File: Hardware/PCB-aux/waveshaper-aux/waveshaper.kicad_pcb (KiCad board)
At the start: 2 copper layers, 189 x 174 mm, 50 parts, among them J1 AudioJack2_SwitchT, J10 2x7 IDC header, J11 Conn_01x03, J12 Conn_01x02, J13 EURO_PWR_2x5, J14 Conn_01x9, J15 Conn_01x9, J2 AudioJack2_SwitchT, J20 Conn_01x02, J3 AudioJack2_SwitchT, J30 2x5 pin socket, J4 AudioJack2_SwitchT, J5 AudioJack2_SwitchT, J6 AudioJack2_SwitchT, J7 AudioJack2_SwitchT, J8 AudioJack2_SwitchT, J9 AudioJack2_SwitchT, SW1 SW_SPDT, U4 4066, U5 4066

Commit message: PCB tweak, font correction on panel
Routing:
- net Net-(D4-Pad2): track 201.4 -> 192.1 mm
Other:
- board text added: "+1"
- board text added: "+10V"
- board text added: "+2"
- board text added: "+3"
- board text added: "-1"
- board text added: "-2"
- board text added: "-3"
- board text added: "0"
- board text added: "GND"

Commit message: Final tweaks before fabbing; Kosmo_panel lib update
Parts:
- added GRAF1: CC0 logo, ao_tht:CC0_logo, B.Cu at (145.5, 55.8)
- renumbered C14 to C1, C15 to C2, C16 to C3, C17 to C4, D4 to D1, D5 to D4, D6 to D5, D7 to D6, D8 to D7, D9 to D8, D10 to D9, J10 to J1, J4 to J10, J5 to J12, J30 to J13, J6 to J14, J7 to J15, J8 to J16, J9 to J17, J1 to J2, J2 to J3, J12 to J4, J13 to J5, J3 to J6, J14 to J7, J20 to J8, J15 to J9, R8 to R1, R9 to R2, R10 to R3, R11 to R4, R12 to R5, R13 to R6, R14 to R7, R25 to R8, R26 to R9, RV8 to RV2, RV2 to RV3, RV3 to RV4, RV4 to RV5, RV5 to RV6, RV6 to RV7, RV7 to RV8, U5 to U1, U4 to U2
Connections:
- J10 pad S: GND -> GND1
- J12 pad S: GND -> GND1
- J14 pad S: GND -> GND1
- J15 pad S: GND -> GND1
- J16 pad S: GND -> GND1
- J17 pad S: GND -> GND1
- J2 pad S: GND -> GND1
- J3 pad S: GND -> GND1
- J6 pad S: GND -> GND1
- J7 pad 1: GND -> GND1
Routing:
- added copper zone on B.Cu, net GND1
- added copper zone on F.Cu, net GND1
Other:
- rule pad_to_mask_clearance: 0.05 -> 0
- board text added: "VCA/pot/switch board Rich Holmes Oct 2020 CC0"
- board text added: "Voltage Controlled 4046 Wave Shaper"
- board text removed: "Voltage Controlled 4046 Wave Shaper VCA/pot/switch board Rich Holmes Oct 2020"

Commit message: Gerbers
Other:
- board text added: "https://github.com/holmesrichards/WaveShaper"

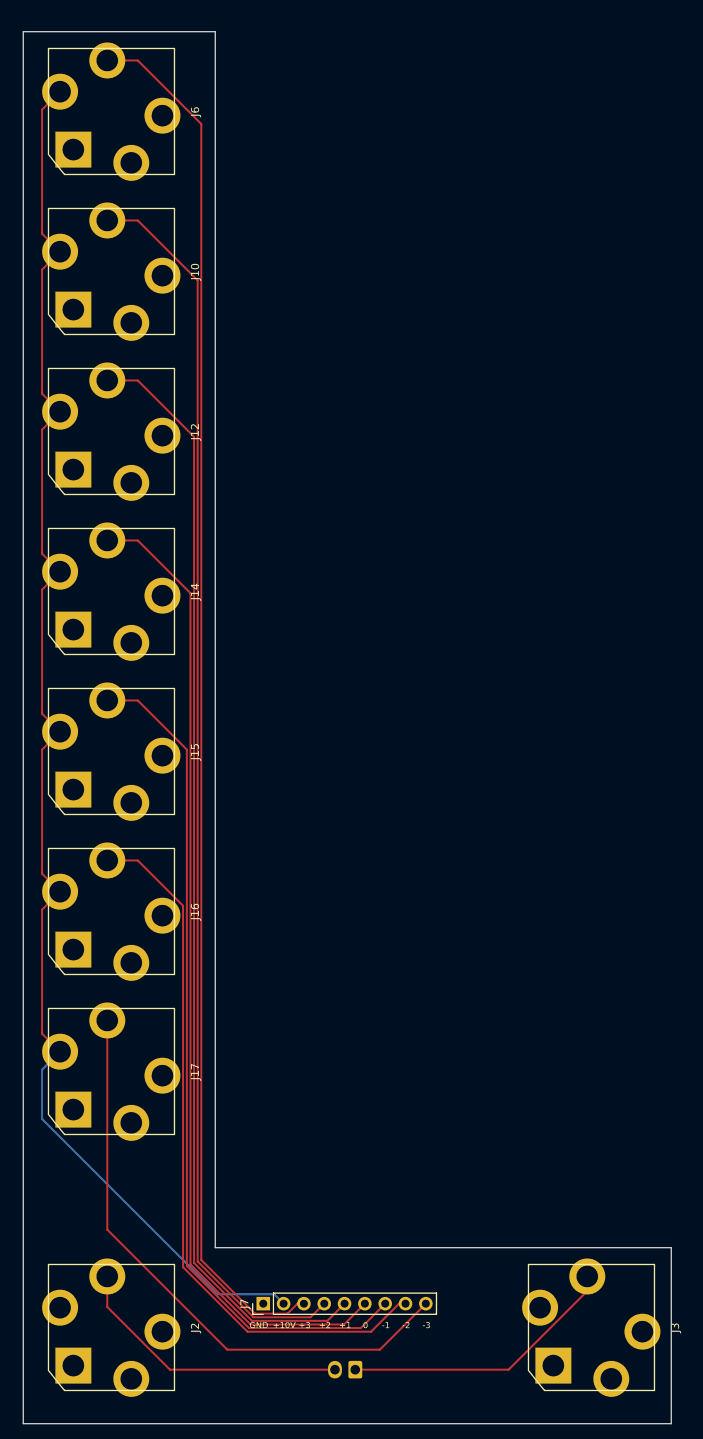
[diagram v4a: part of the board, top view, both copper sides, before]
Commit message: Documentation, some cosmetic sch/PCB changes
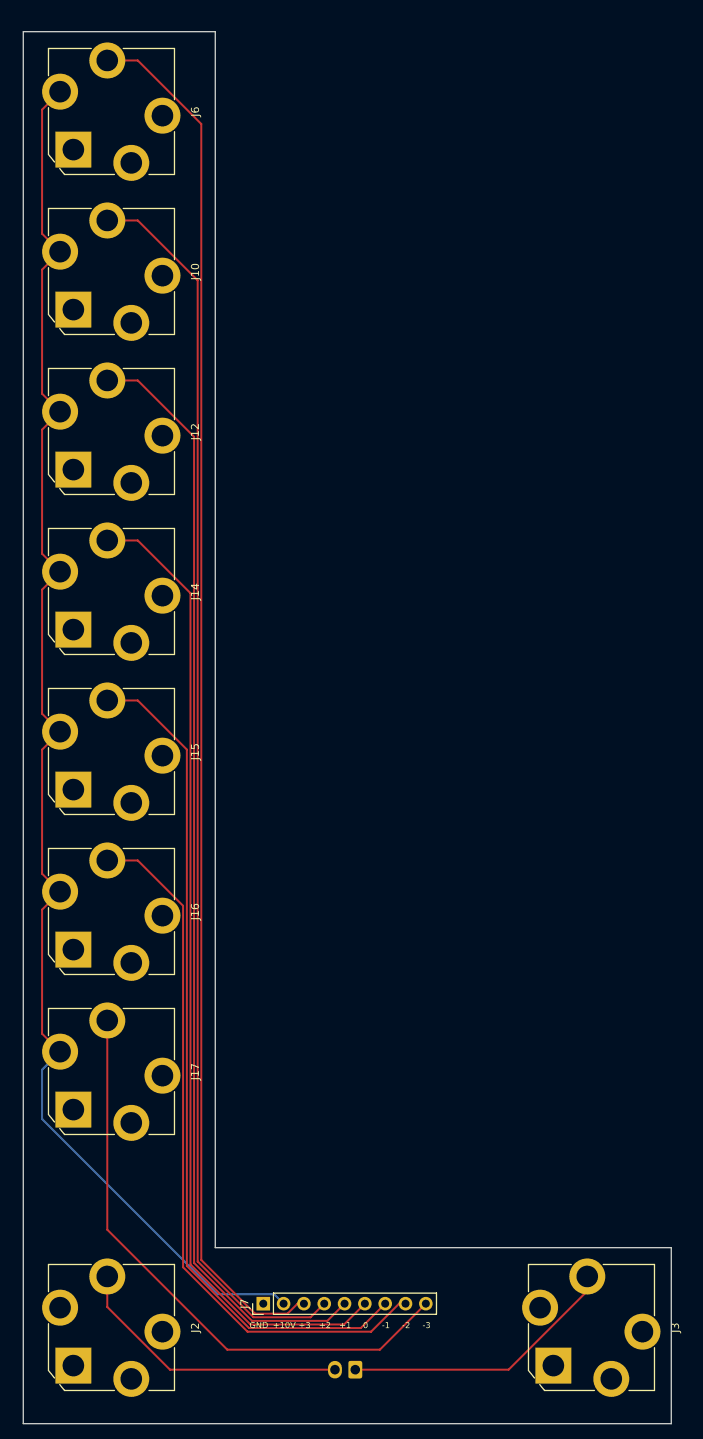
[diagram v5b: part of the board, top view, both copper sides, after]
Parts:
- J11: value Conn_01x03 -> 3_pin_Molex_header
- J4, J8: value Conn_01x02 -> 2_pin_Molex_header

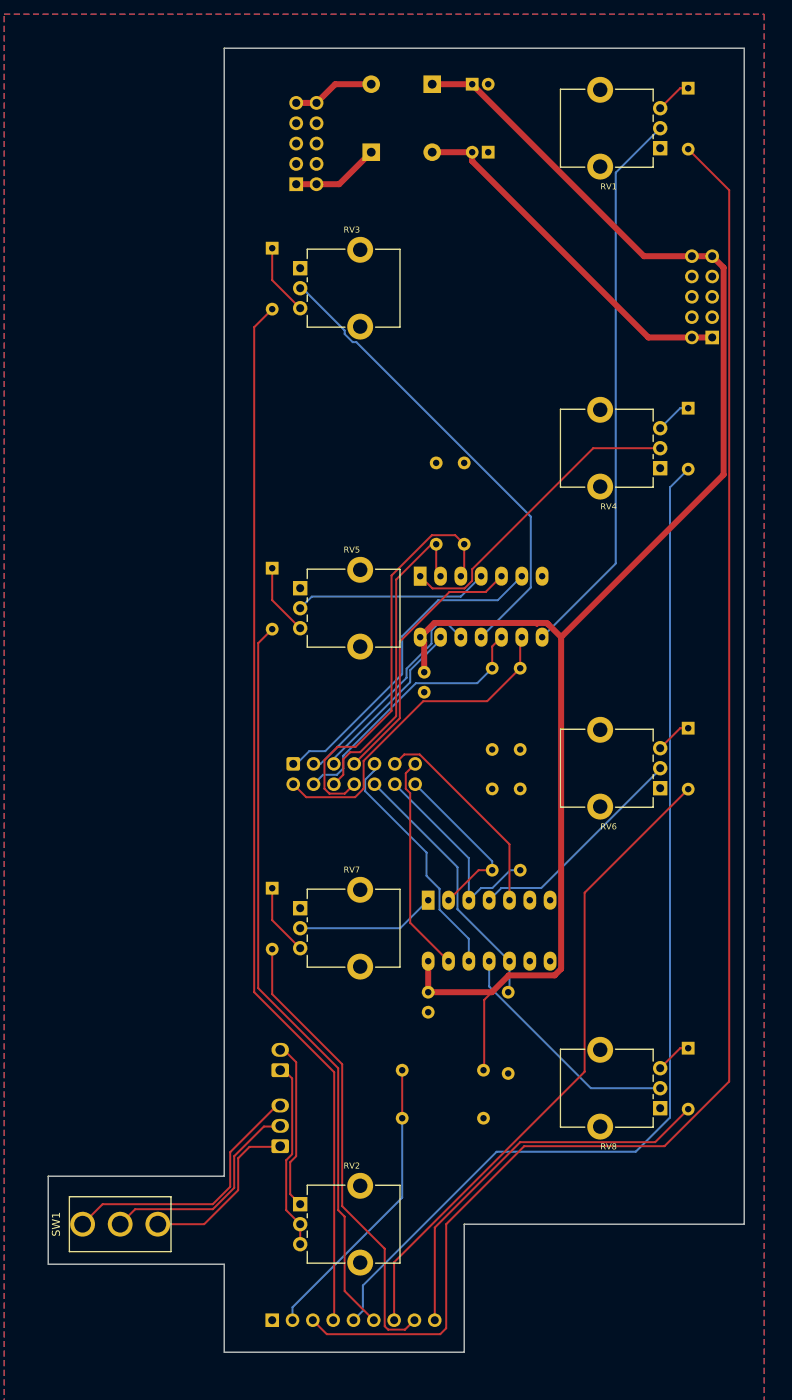
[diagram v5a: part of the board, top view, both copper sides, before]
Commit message: Mounting hole; parallel Schottkys instead of series switchers
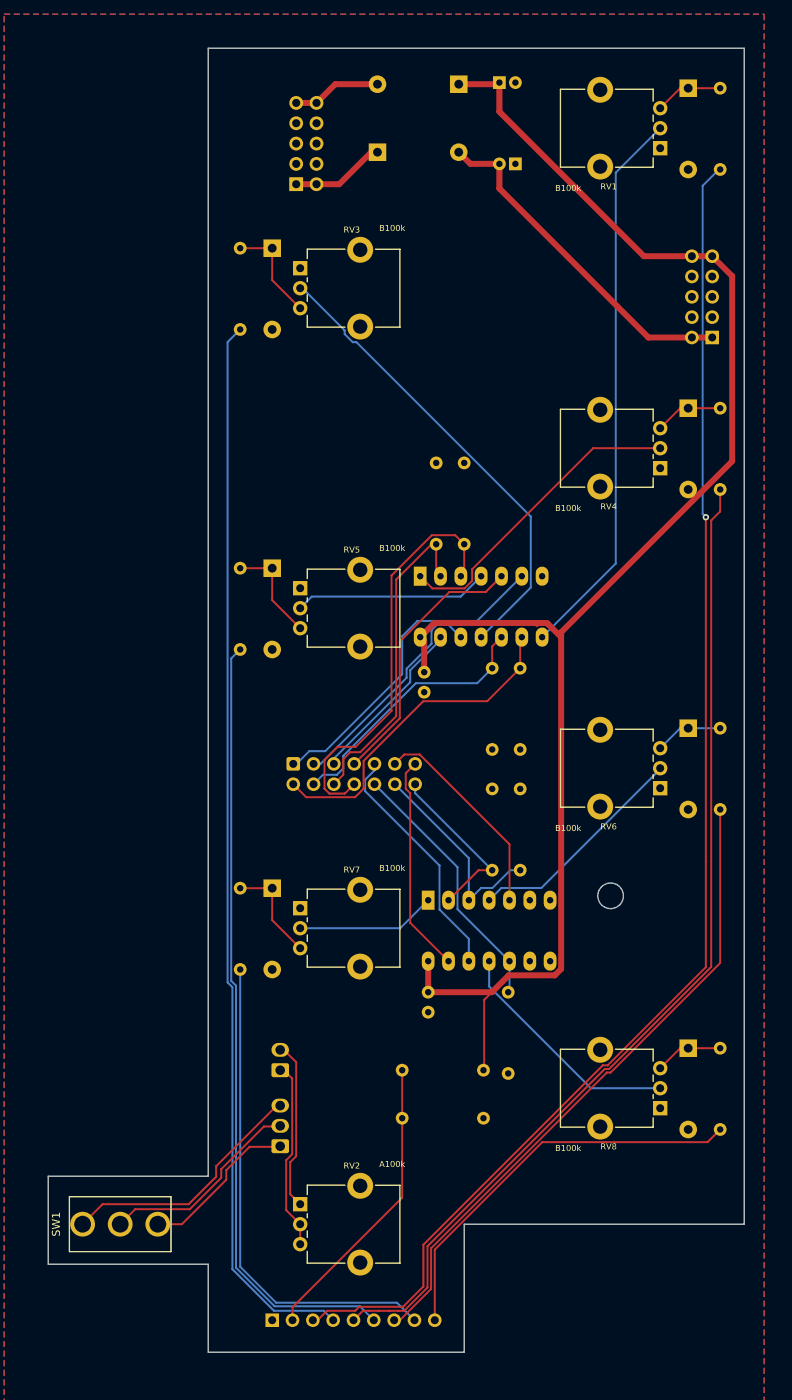
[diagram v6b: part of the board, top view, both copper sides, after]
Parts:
- removed the D4 at (120.0, 44.0)
- added D2: 1N5817, ao_tht:D_DO-41_SOD81_P10.16mm_Horizontal, B.Cu at (120.0, 44.0)
- added H1: MountingHole, ao_tht:MountingHole_3.2mm_M3, F.Cu at (162.3, 125.0)
- added R10: 1k, ao_tht:R_Axial_DIN0207_L6.3mm_D2.5mm_P10.16mm_Horizontal, B.Cu at (176.0, 34.2)
- added R11: 1k, ao_tht:R_Axial_DIN0207_L6.3mm_D2.5mm_P10.16mm_Horizontal, B.Cu at (116.0, 44.0)
- added R12: 1k, ao_tht:R_Axial_DIN0207_L6.3mm_D2.5mm_P10.16mm_Horizontal, B.Cu at (176.0, 64.0)
- added R13: 1k, ao_tht:R_Axial_DIN0207_L6.3mm_D2.5mm_P10.16mm_Horizontal, B.Cu at (116.0, 84.0)
- added R14: 1k, ao_tht:R_Axial_DIN0207_L6.3mm_D2.5mm_P10.16mm_Horizontal, B.Cu at (176.0, 104.0)
- added R15: 1k, ao_tht:R_Axial_DIN0207_L6.3mm_D2.5mm_P10.16mm_Horizontal, B.Cu at (116.0, 124.0)
- added R16: 1k, ao_tht:R_Axial_DIN0207_L6.3mm_D2.5mm_P10.16mm_Horizontal, B.Cu at (176.0, 144.0)
- D1, D5, D6, D7, D8, D9: value 1N4148 -> 1N5817; footprint ao_tht:D_DO-35_SOD27_P7.62mm_Horizontal -> ao_tht:D_DO-41_SOD81_P10.16mm_Horizontal
- D3: renamed from D2; footprint ao_tht:D_DO-41_SOD81_P7.62mm_Horizontal -> ao_tht:D_DO-41_SOD81_P10.16mm_Horizontal
- D4: renamed from D3; footprint ao_tht:D_DO-41_SOD81_P7.62mm_Horizontal -> ao_tht:D_DO-41_SOD81_P10.16mm_Horizontal
- moved C2 3.70 mm to (150.4, 33.5)
- moved C1 3.41 mm to (148.4, 23.3)
- moved D3 3.32 mm to (143.3, 23.5)
- moved D4 0.78 mm to (133.2, 32.0)
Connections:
- D1 pad 2: Net-(D1-Pad2) -> GND
- D5 pad 2: Net-(D5-Pad2) -> GND
- D6 pad 2: Net-(D6-Pad2) -> GND
- D7 pad 2: Net-(D7-Pad2) -> GND
- D8 pad 2: Net-(D8-Pad2) -> GND
- D9 pad 2: Net-(D9-Pad2) -> GND
- J9 pad 3: Net-(D1-Pad2) -> Net-(J9-Pad3)
- J9 pad 5: Net-(D5-Pad2) -> Net-(J9-Pad5)
- J9 pad 6: Net-(D6-Pad2) -> Net-(J9-Pad6)
- J9 pad 7: Net-(D7-Pad2) -> Net-(J9-Pad7)
- J9 pad 8: Net-(D8-Pad2) -> Net-(J9-Pad8)
- J9 pad 9: Net-(D9-Pad2) -> Net-(J9-Pad9)
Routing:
- net Net-(D1-Pad2): track 192.1 -> 0.00 mm
- net Net-(J9-Pad3): track 0.00 -> 171.4 mm, vias 0 -> 1
- net Net-(D5-Pad2): track 133.9 -> 0.00 mm
- net Net-(J9-Pad5): track 0.00 -> 126.2 mm
- net Net-(J9-Pad6): track 0.00 -> 97.9 mm
- net Net-(D6-Pad2): track 93.1 -> 0.00 mm
- net Net-(D7-Pad2): track 81.6 -> 0.00 mm
- net Net-(J9-Pad7): track 0.00 -> 81.4 mm
- net Net-(J9-Pad8): track 0.00 -> 61.7 mm
- net Net-(D8-Pad2): track 57.3 -> 0.00 mm
- net Net-(J9-Pad9): track 0.00 -> 50.7 mm
- net Net-(D9-Pad2): track 49.4 -> 0.00 mm
- net Net-(D9-Pad1): track 4.54 -> 8.54 mm
- net Net-(D8-Pad1): track 8.95 -> 12.9 mm
- net Net-(D7-Pad1): track 4.54 -> 8.54 mm
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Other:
- outline, holes or cut-outs redrawn

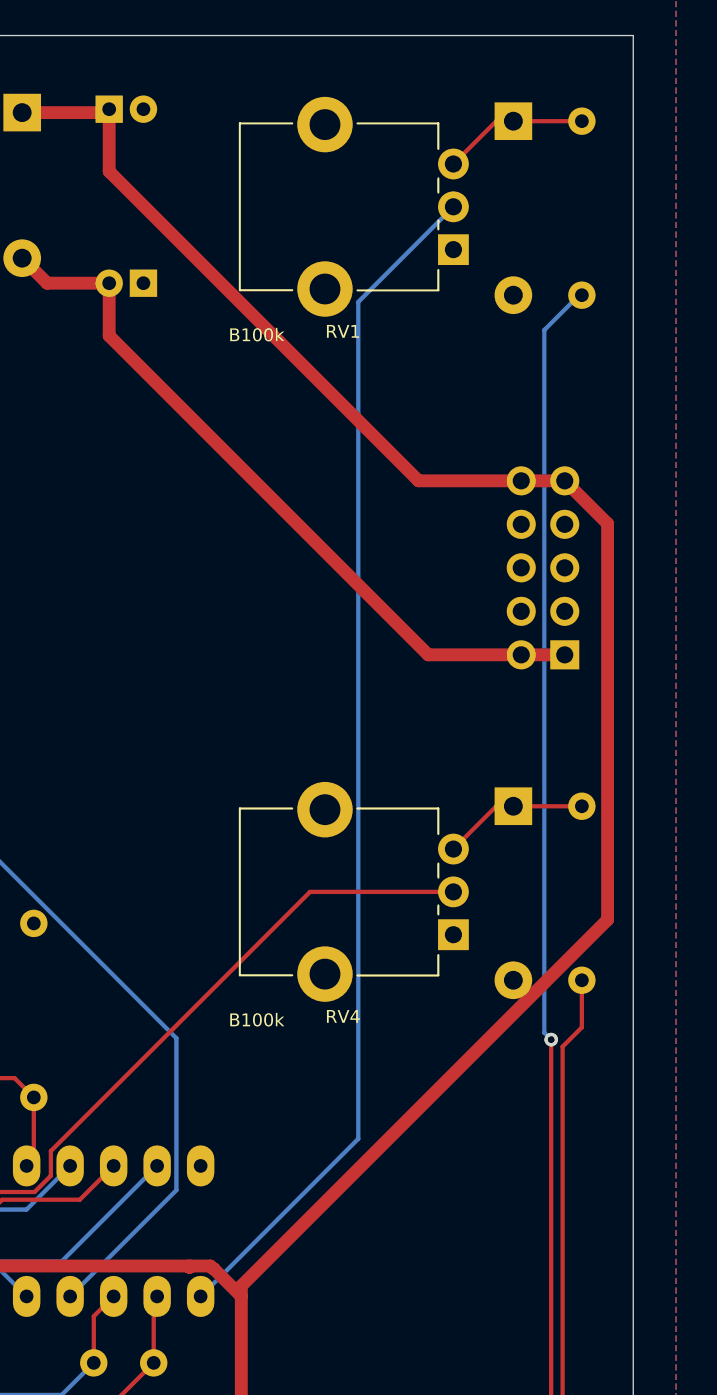
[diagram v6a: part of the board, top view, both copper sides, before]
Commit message: Fix power polarity
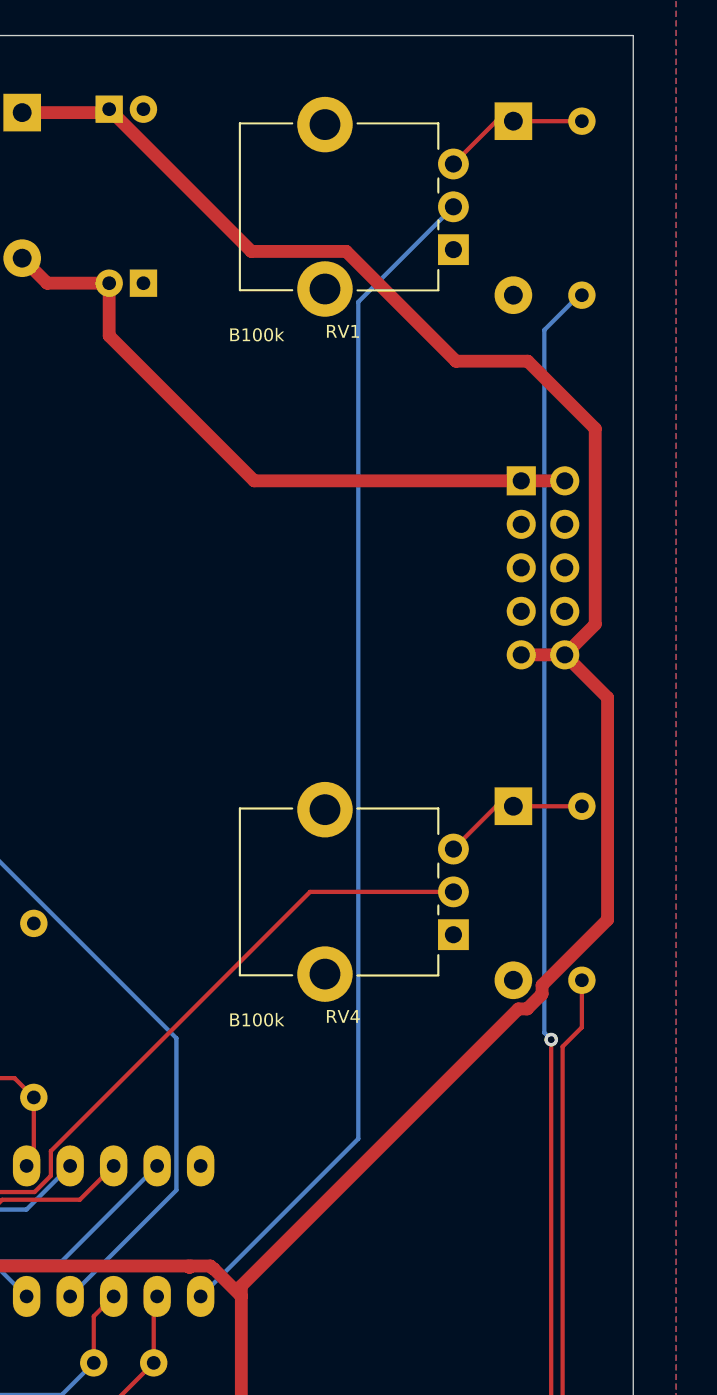
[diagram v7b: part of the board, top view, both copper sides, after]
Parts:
- moved J13 10.5 mm to (172.5, 45.0), turned to 180 degrees
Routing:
- net +12V: track 197.5 -> 202.5 mm
- net -12V: track 43.1 -> 38.9 mm
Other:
- board text added: "+12V"
- board text added: "-12V"

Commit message: Docs and minor corrections
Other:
- board text added: "Rich Holmes Sep 2021"
- board text added: "VCA/pot/switch board Rich Holmes Sep 2021 CC0"
- board text removed: "Rich Holmes Oct 2020"
- board text removed: "VCA/pot/switch board Rich Holmes Oct 2020 CC0"
